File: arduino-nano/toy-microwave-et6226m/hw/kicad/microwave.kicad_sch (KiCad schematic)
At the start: 64 parts, among them J1 Screw_Terminal_01x04, J2 Screw_Terminal_01x04, Q2 AO3400A, U1 AP63205WU, U2 CC56-12SURKWA, U5 ET6226M

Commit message: refactor(arduino-nano): move both boards into symmetric fw/ and hw/ packages
- What: moves each KiCad project to hw/kicad/, datasheets to hw/datasheets/, the microwave enclosure DXF to hw/mech/enclosure-template.dxf, and the microwave firmware into fw/, and deletes the stale microwave.csv, microwave.net, and toy-microwave.pdf exports.
- Why: the two boards used different layouts, and generated files sat beside the KiCad sources with no way to rebuild them.
- How: writes MPN, Manufacturer, Digi-Key, Mouser, and LCSC fields from parts.csv into every schematic symbol and PCB footprint, marks the Nano and MX switches Exclude from BOM per the part policy, gives the dimmer a rev 1 title block, points its sym-lib-table at kicad/embedded.kicad_sym, and adds one ../ to the microwave lib_deps.
- Benefit: both boards share one layout, each schematic carries its own purchasing data, and the microwave firmware still builds with 31 of 31 native tests passing.
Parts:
- A1, MX1, MX10, MX11, MX12, MX13, MX14, MX15, MX16, MX2, MX3, MX4, MX5, MX6, MX7, MX8, MX9: now left out of the parts list
- BZ1: Digi-Key (none) -> 433-1028-ND; MPN (none) -> WT-1205; Manufacturer (none) -> Soberton Inc.
- C1, C2: Digi-Key (none) -> 399-C0805C101J1GAC7210CT-ND; MPN (none) -> C0805C101J1GAC7210; Manufacturer (none) -> KEMET; Mouser (none) -> 80-C0805C101J1G7210
- C3: Digi-Key (none) -> 399-6929-1-ND; MPN (none) -> C0805C105K3RACAUTO; Manufacturer (none) -> KEMET; Mouser (none) -> 80-C0805C105K3RAUTO
- C4: Digi-Key (none) -> 587-TMK325AB7106MMHPRCT-ND; MPN (none) -> TMK325AB7106MMHPR; Manufacturer (none) -> Taiyo Yuden; Mouser (none) -> 963-TMK325AB7106MMPR
- C5: Digi-Key (none) -> 399-12977-1-ND; MPN (none) -> C0805C104M5RACAUTO; Manufacturer (none) -> KEMET; Mouser (none) -> 80-C0805C104M5RAUTO
- C6, C7: Digi-Key (none) -> 1276-3373-1-ND; MPN (none) -> CL32A226MAJNNNE; Manufacturer (none) -> Samsung; Mouser (none) -> 187-CL32A226MAJNNNE
- D1, D10, D11, D12, D13, D14, D15, D16, D2, D3, D4, D5, D6, D7, D8, D9: Digi-Key (none) -> 1N4148W-FDICT-ND; MPN (none) -> 1N4148W-7-F; Manufacturer (none) -> Diodes Inc; Mouser (none) -> 621-1N4148W-F
- D17, D18: Digi-Key (none) -> SS14-E3/61TGICT-ND; MPN (none) -> SS14-E3/61T; Manufacturer (none) -> Vishay; Mouser (none) -> 625-SS14-E3
- J1, J2: Digi-Key (none) -> 277-1265-ND; MPN (none) -> 1715747; Manufacturer (none) -> Phoenix Contact; Mouser (none) -> 651-1715747
- L1: Digi-Key (none) -> 490-LQH55DN4R7M03LCT-ND; MPN (none) -> LQH55DN4R7M03L; Manufacturer (none) -> Murata; Mouser (none) -> 81-LQH55DN4R7M03L
- Q2: Digi-Key (none) -> 785-1000-1-ND; MPN (none) -> AO3400A; Manufacturer (none) -> Alpha & Omega
- R1, R2, R3, R4: Digi-Key (none) -> 311-2.00KCRCT-ND; MPN (none) -> RC0805FR-072KL; Manufacturer (none) -> Yageo; Mouser (none) -> 603-RC0805FR-072KL
- R10, R7, R8: Digi-Key (none) -> 311-4.70KCRCT-ND; MPN (none) -> RC0805FR-074K7L; Manufacturer (none) -> Yageo; Mouser (none) -> 603-RC0805FR-074K7L
- R5, R6, R9: Digi-Key (none) -> 311-100CRCT-ND; MPN (none) -> RC0805FR-07100RL; Manufacturer (none) -> Yageo; Mouser (none) -> 603-RC0805FR-07100RL
- U1: Digi-Key (none) -> AP63205WU-7DICT-ND; MPN (none) -> AP63205WU-7; Manufacturer (none) -> Diodes Inc; Mouser (none) -> 621-AP63205WU-7
- U2: Digi-Key (none) -> 754-CC56-12SURKWA-ND; MPN (none) -> CC56-12SURKWA; Manufacturer (none) -> Kingbright; Mouser (none) -> 604-CC5612SURKWA
- U5: Digi-Key (none) -> 4518-ET6226MCT-ND; MPN (none) -> ET6226M; Manufacturer (none) -> UMW

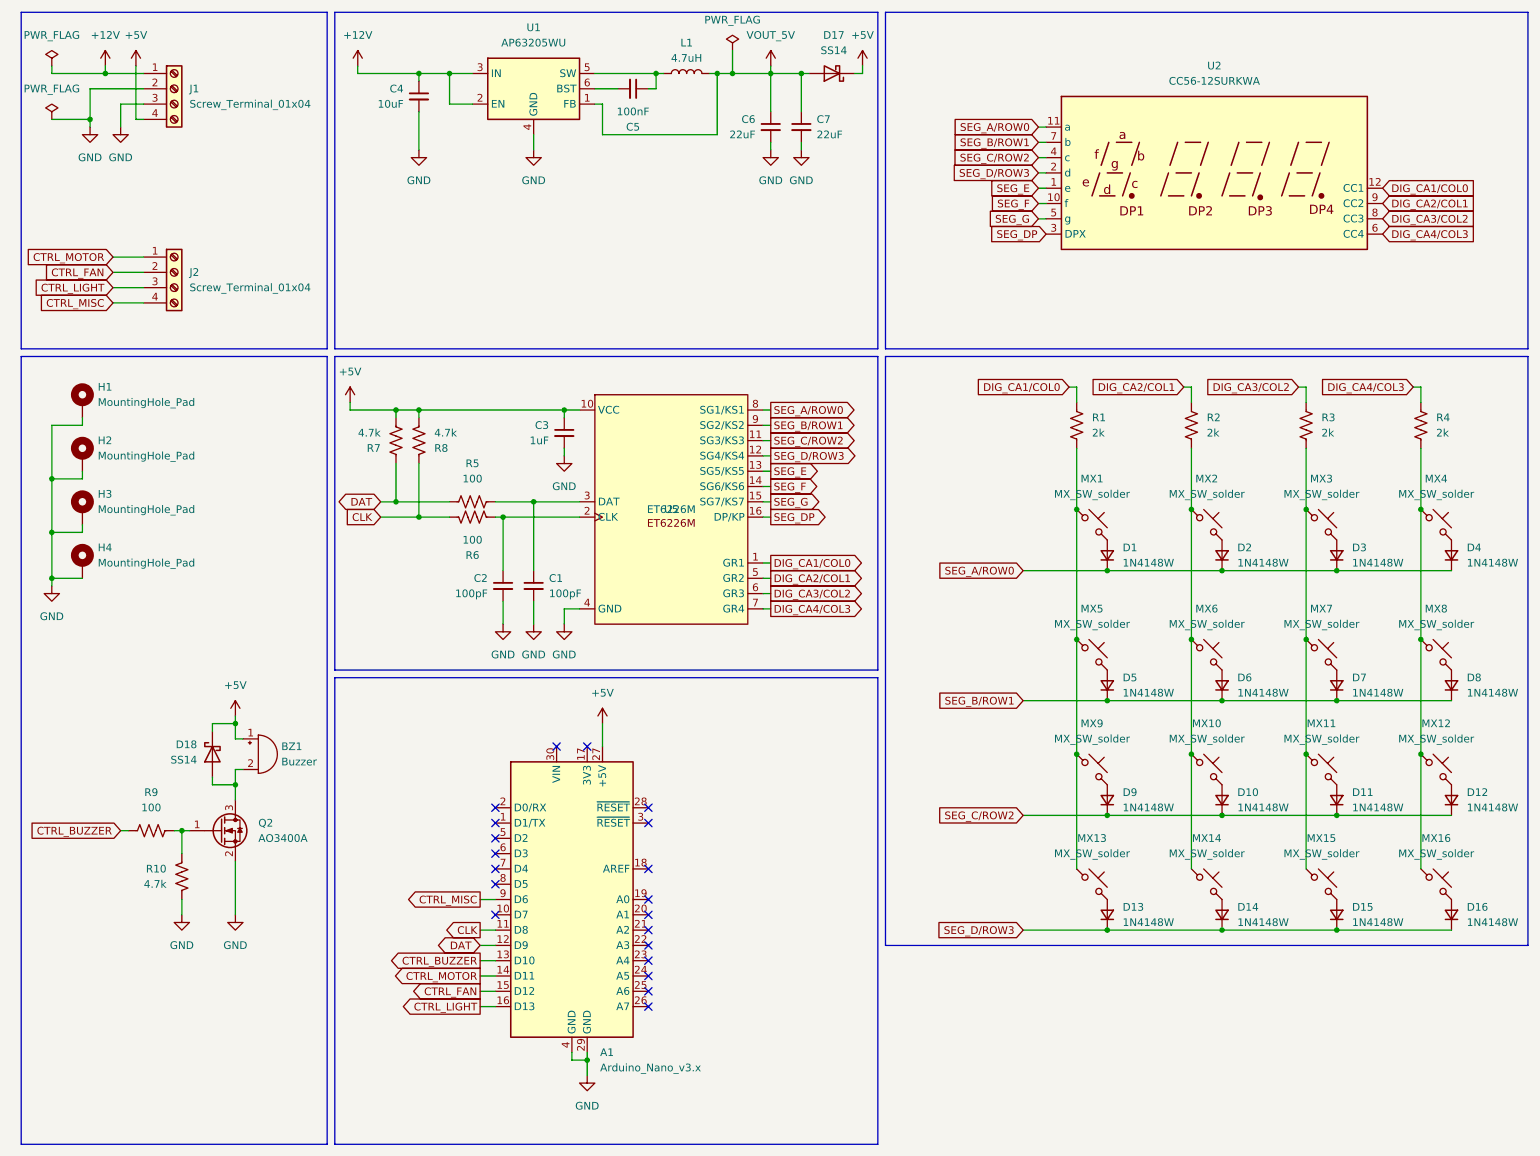
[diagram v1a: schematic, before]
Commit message: feat(toy-microwave-et6226m): make J2 a grounded logic header with pull-downs
- What: reorders J2 to LIGHT, MOTOR, FAN, GND, moves CTRL_LIGHT to D10 and CTRL_BUZZER to D6, adds 10 kOhm pull-downs R11-R13 on the three control lines, and marks D13 no-connect.
- Why: J2 had no ground for off-board peripheral boards to reference, and the control lines floated while the Nano was in reset.
- How: replaced CTRL_MISC on pin 4 with GND, placed and routed R11-R13 as RC0805FR-0710KL, and kept outputs logic-level so each peripheral owns its driver and power.
- Benefit: any peripheral board can take its signals and ground from one connector and sees every line held low through reset, with ERC clean and 0 unconnected pads.
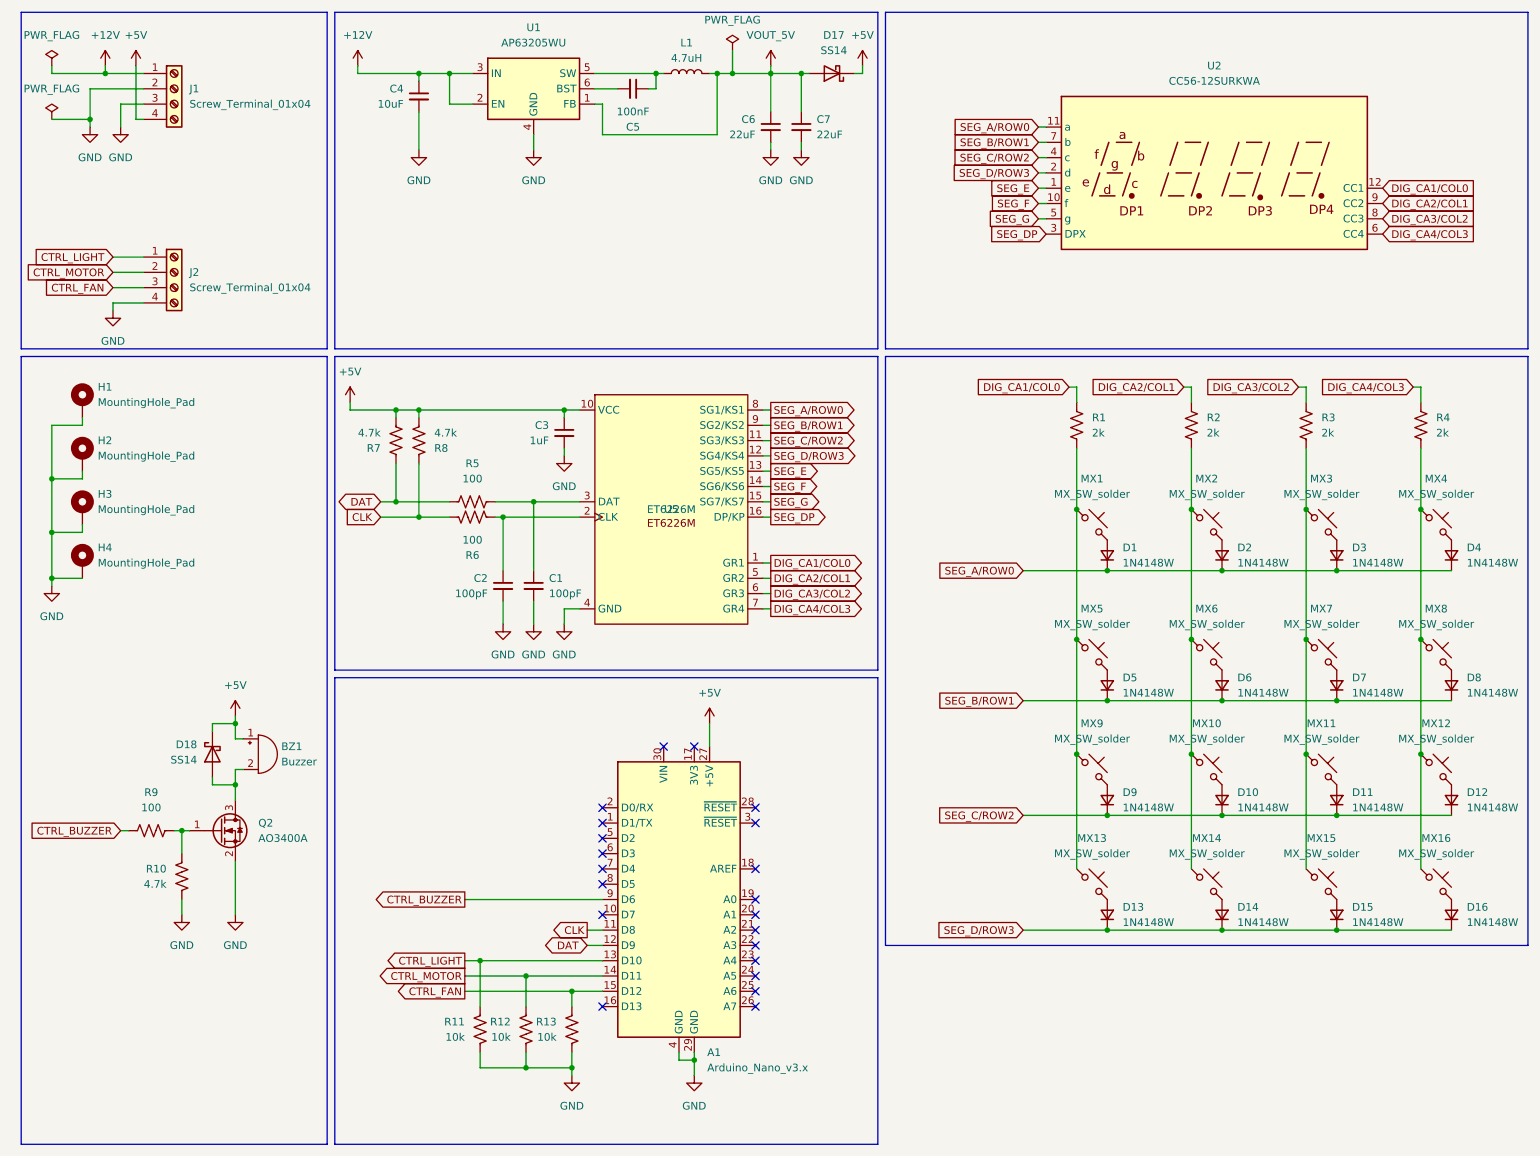
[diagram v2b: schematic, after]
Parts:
- added R11, R12, R13: 10k, Resistor_SMD:R_0805_2012Metric_Pad1.20x1.40mm_HandSolder, symbol Device:R_US
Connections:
- net CTRL_BUZZER: now also A1.9 (D6); no longer A1.13 (D10)
- net CTRL_FAN: now also J2.3 (Pin_3), R13.2; no longer J2.2 (Pin_2)
- net CTRL_LIGHT: now also A1.13 (D10), J2.1 (Pin_1), R11.2; no longer A1.16 (D13), J2.3 (Pin_3)
- net CTRL_MOTOR: now also J2.2 (Pin_2), R12.2; no longer J2.1 (Pin_1)
- net GND: now also J2.4 (Pin_4), R11.1, R12.1, R13.1
- removed net CTRL_MISC: A1.9 (D6), J2.4 (Pin_4)
- no-connect marks 20 -> 21
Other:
- moved on the sheet: A1
